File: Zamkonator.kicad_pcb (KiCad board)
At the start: 2 copper layers, 75 x 75 mm, 100 parts, among them J1 Screw_Terminal_01x06, J2 RJ45_Abracon_ARJP11A-MASA-B-A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, J3 Conn_01x08_Male, J4 Conn_02x08_Counter_Clockwise, K1 SRD-DC3V-SL-C, Q1 BCP56, T1 HR051142, U1 RTL8201F, U2 SI3404-A-GM, U3 EL3H7-G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

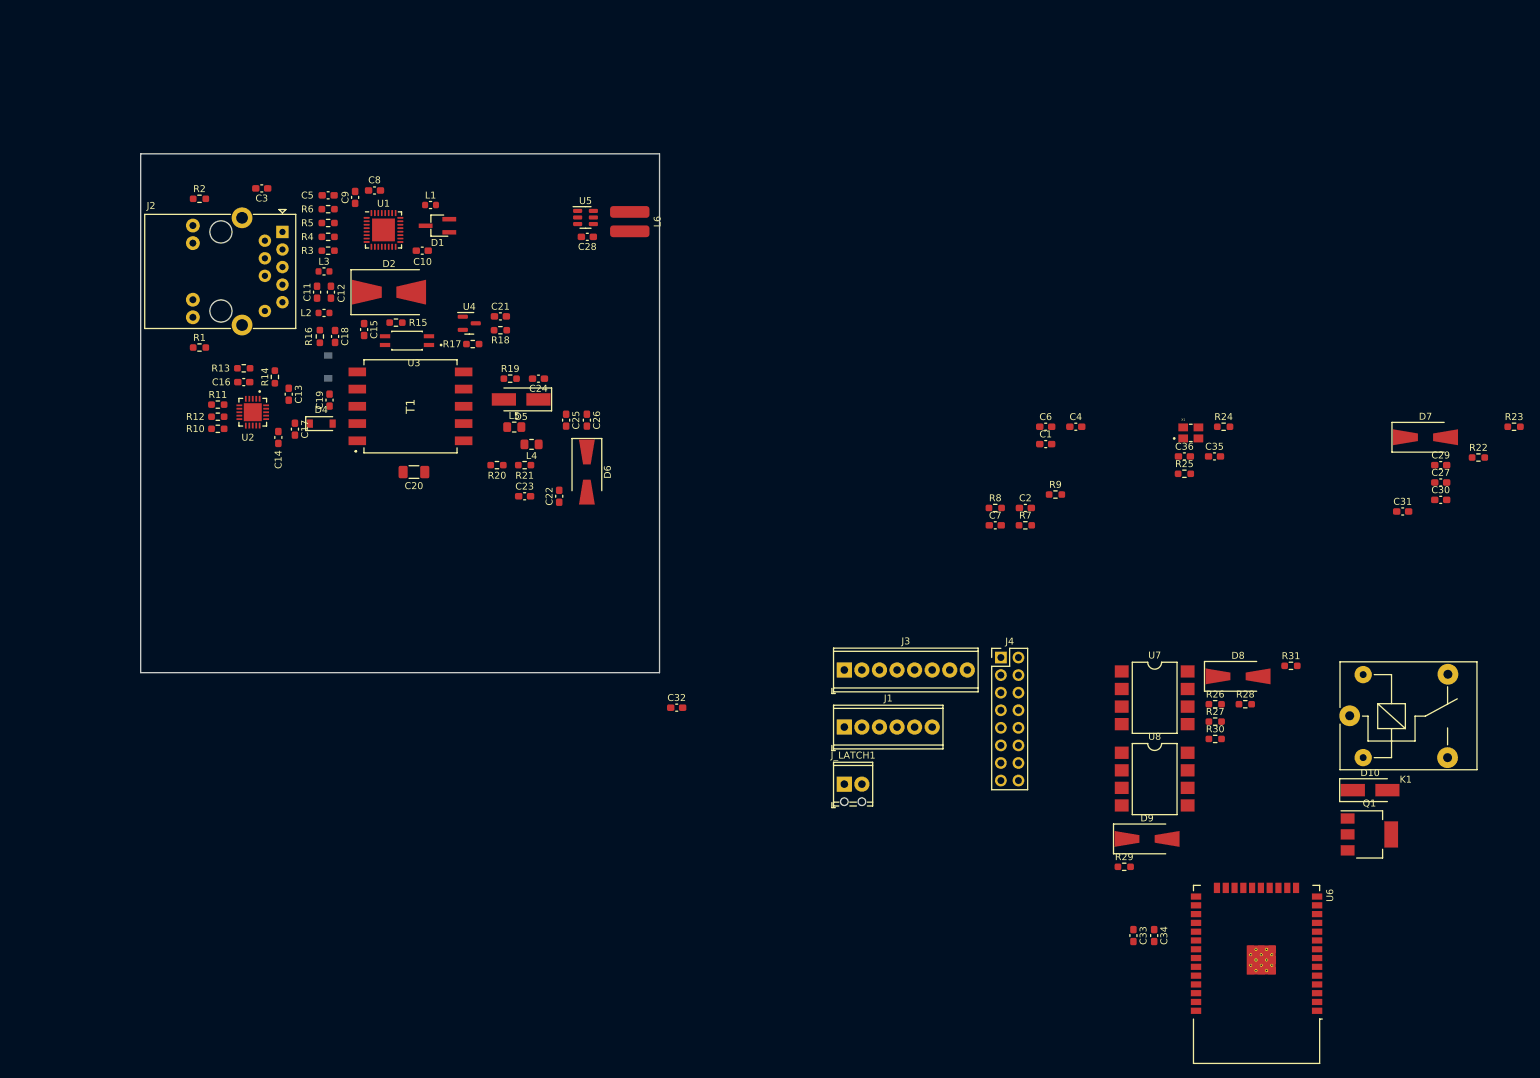
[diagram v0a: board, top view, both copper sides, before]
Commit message: layout fixes
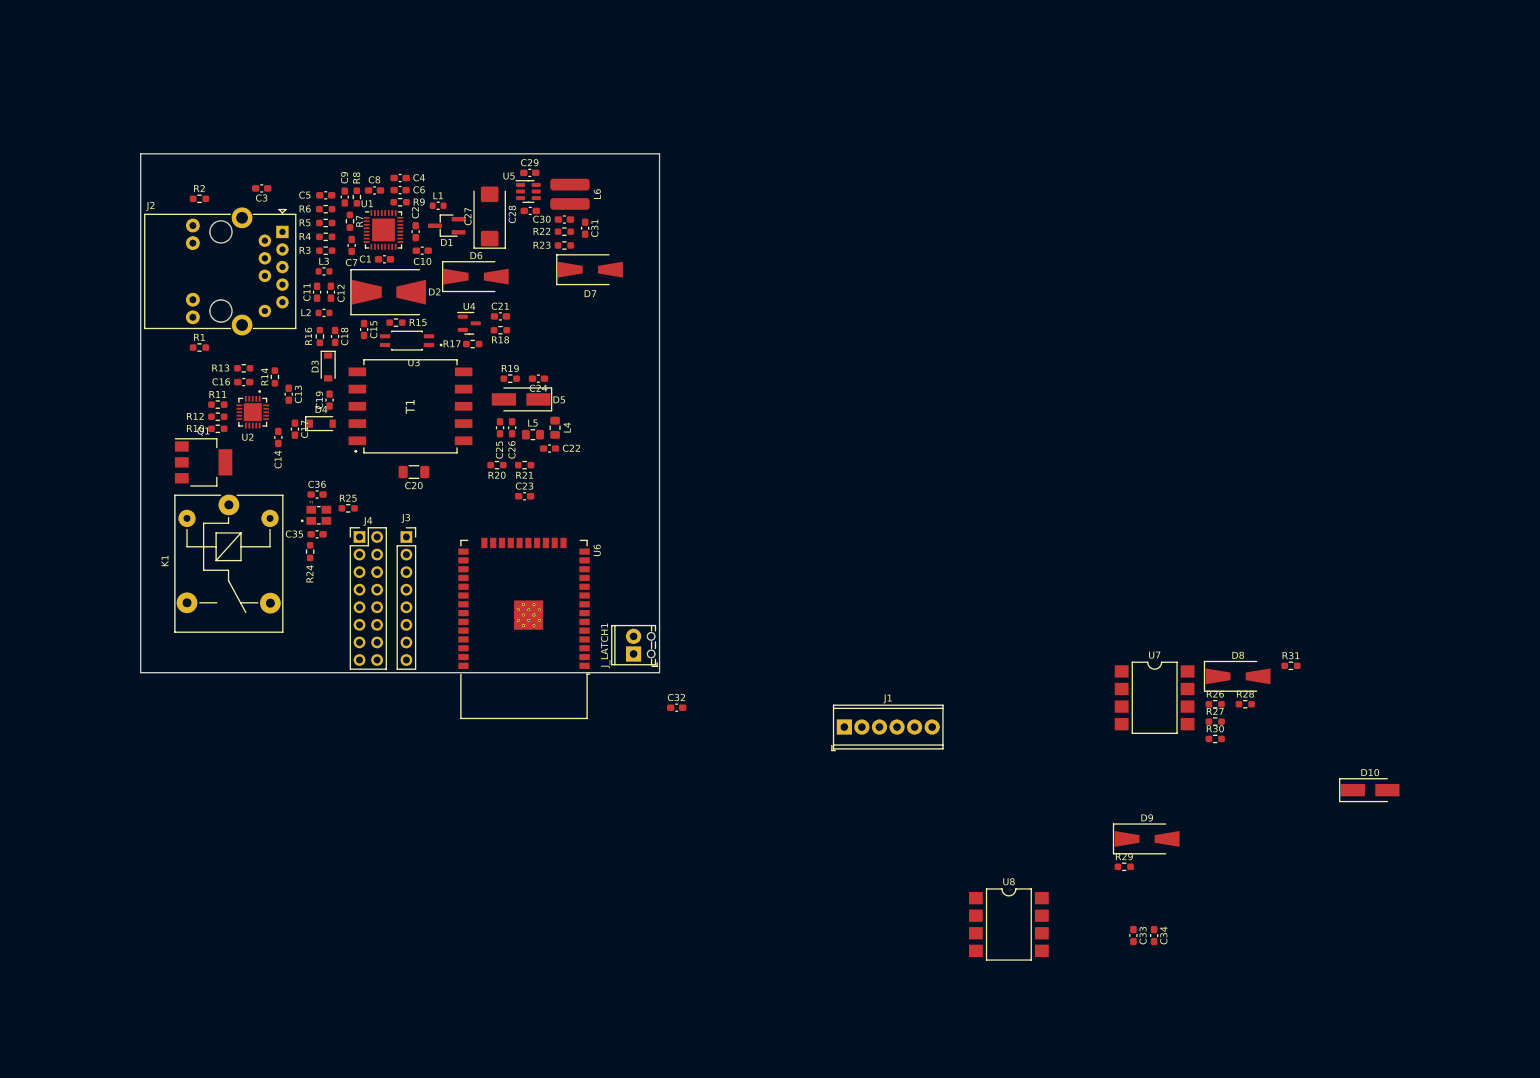
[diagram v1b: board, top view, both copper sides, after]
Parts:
- C27: footprint Capacitor_SMD:C_0603_1608Metric_Pad1.08x0.95mm_HandSolder -> Capacitor_Tantalum_SMD:CP_EIA-7343-30_AVX-N_Pad2.25x2.55mm_HandSolder
- D3: moved to F.Cu
- J3: footprint TerminalBlock_Phoenix:TerminalBlock_Phoenix_MPT-0,5-8-2.54_1x08_P2.54mm_Horizontal -> Connector_PinSocket_2.54mm:PinSocket_1x08_P2.54mm_Vertical
- moved Q1 176.9 mm to (25.6, 63.6)
- moved K1 164.9 mm to (29.2, 69.8), turned to -90 degrees
- moved C27 142.7 mm to (67.0, 28.1), turned to 90 degrees
- moved R23 139.7 mm to (77.8, 32.2)
- moved C29 138.3 mm to (72.8, 21.8)
- moved R22 136.1 mm to (77.8, 30.2), turned to 180 degrees
- moved R24 133.3 mm to (41.0, 76.5), turned to 90 degrees
- moved C30 133.0 mm to (77.8, 28.5), turned to 180 degrees
- moved C35 130.2 mm to (42.0, 74.0)
- moved X1 126.6 mm to (42.2, 71.2)
- moved C36 125.5 mm to (42.0, 68.2)
- moved C31 125.1 mm to (80.8, 29.8), turned to -90 degrees
- moved D7 123.1 mm to (81.5, 35.8)
- moved R25 121.0 mm to (46.5, 70.2)
- moved U6 117.0 mm to (71.9, 84.8)
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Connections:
- X1 pad 2: (no net) -> GND
- X1 pad 3: (no net) -> Net-(R25-Pad1)
- X1 pad 4: (no net) -> +3.3V

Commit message: Finish basic layout
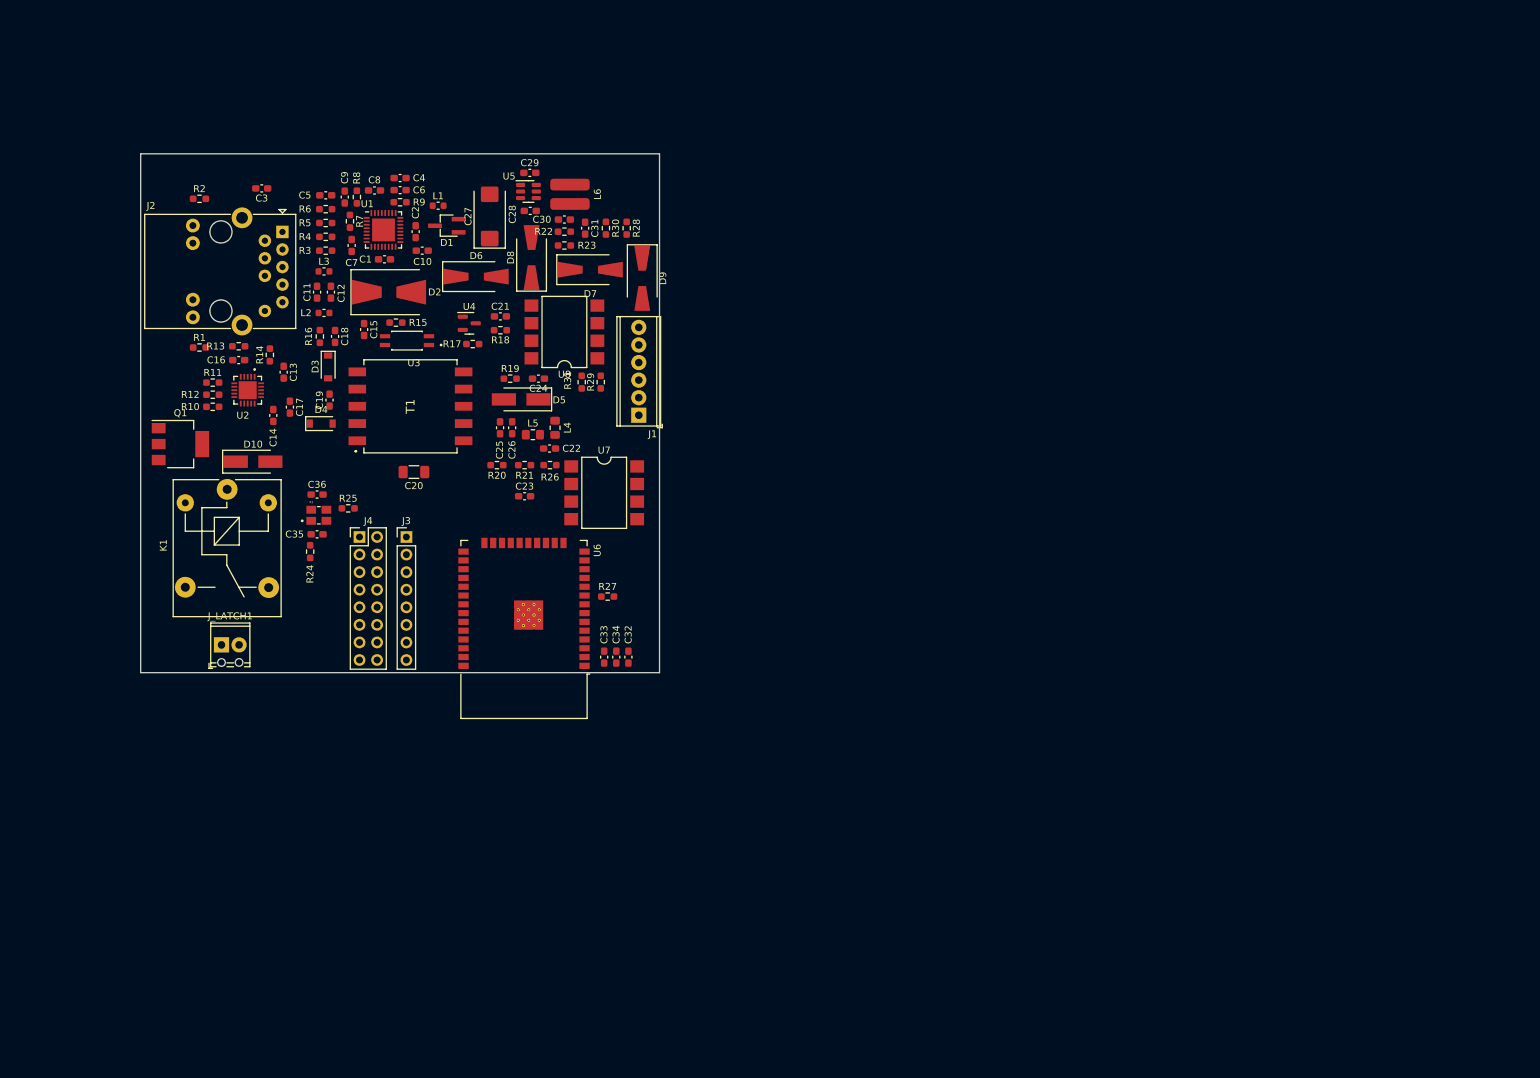
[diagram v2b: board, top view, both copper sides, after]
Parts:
- J3: footprint Connector_PinSocket_2.54mm:PinSocket_1x08_P2.54mm_Vertical -> Connector_PinHeader_2.54mm:PinHeader_1x08_P2.54mm_Vertical
- moved D10 168.3 mm to (32.8, 63.5)
- moved D8 118.7 mm to (73.0, 34.0), turned to 90 degrees
- moved R30 114.9 mm to (83.8, 29.8), turned to -90 degrees
- moved R28 112.8 mm to (86.8, 29.8), turned to -90 degrees
- moved R31 110.4 mm to (80.2, 52.0), turned to -90 degrees
- moved D9 109.0 mm to (89.0, 37.0), turned to -90 degrees
- moved U8 107.1 mm to (77.8, 44.8), turned to 180 degrees
- moved R29 103.1 mm to (83.0, 52.0), turned to 90 degrees
- moved R26 102.2 mm to (75.7, 64.0)
- moved R27 89.7 mm to (84.0, 83.0)
- moved C34 87.6 mm to (85.2, 91.8)
- moved C33 86.4 mm to (83.5, 91.8)
- moved U7 84.9 mm to (83.5, 68.0)
- moved J_LATCH1 59.6 mm to (28.2, 90.0), turned to 0 degrees
- moved J1 54.0 mm to (88.5, 56.8), turned to 90 degrees
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
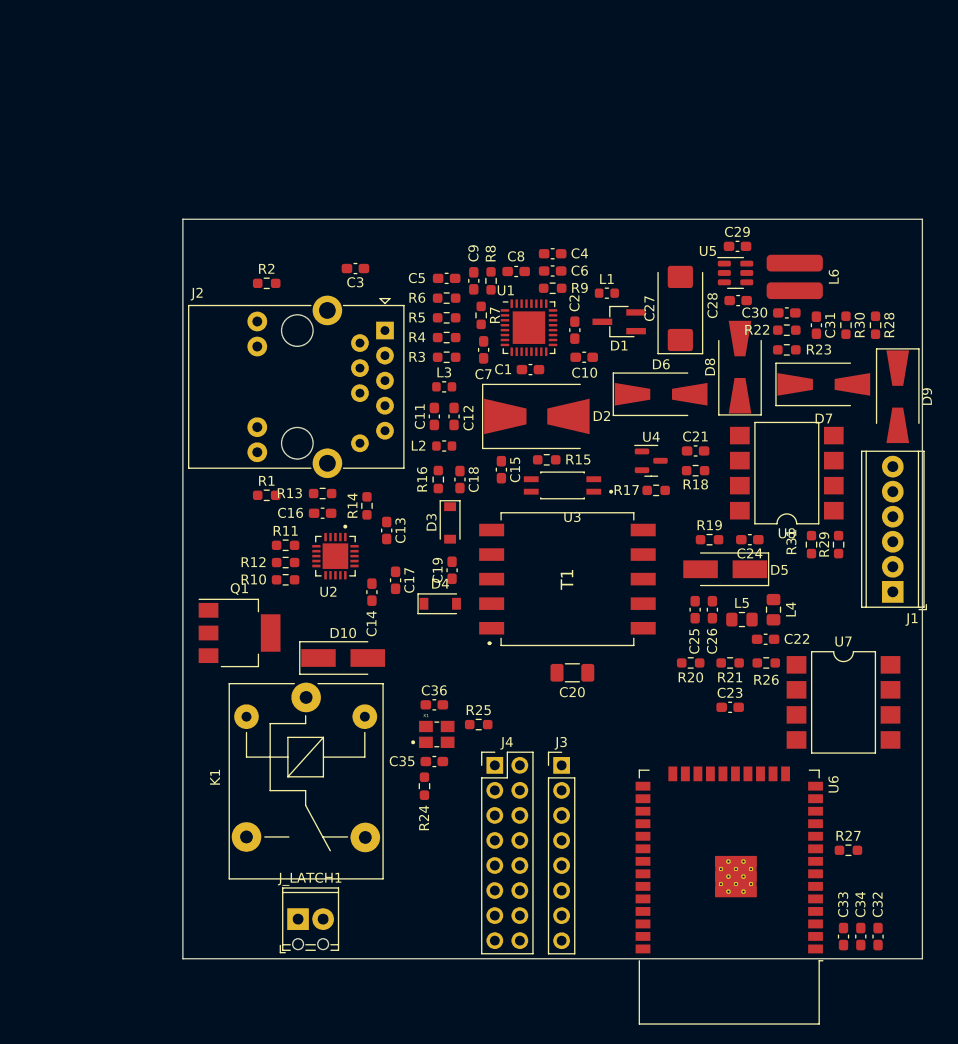
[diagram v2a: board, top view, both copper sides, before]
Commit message: add screw holes
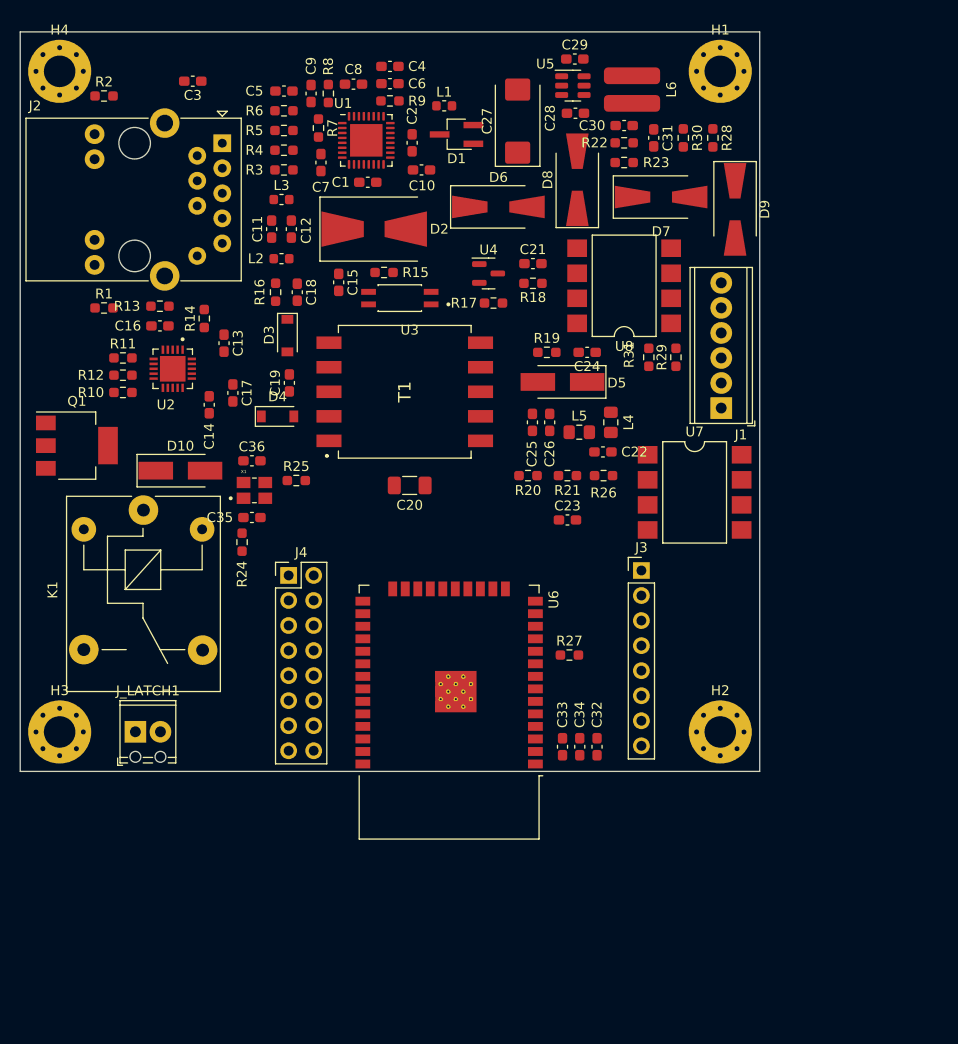
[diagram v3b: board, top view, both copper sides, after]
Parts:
- added H1: MountingHole_Pad, MountingHole:MountingHole_3.2mm_M3_Pad_Via, F.Cu at (71.0, 4.00)
- added H2: MountingHole_Pad, MountingHole:MountingHole_3.2mm_M3_Pad_Via, F.Cu at (71.0, 71.0)
- added H3: MountingHole_Pad, MountingHole:MountingHole_3.2mm_M3_Pad_Via, F.Cu at (4.00, 71.0)
- added H4: MountingHole_Pad, MountingHole:MountingHole_3.2mm_M3_Pad_Via, F.Cu at (4.00, 4.00)
- moved R27 34.5 mm to (55.7, 63.2)
- moved C32 34.4 mm to (58.5, 72.5)
- moved C33 34.4 mm to (55.0, 72.5)
- moved C34 34.4 mm to (56.8, 72.5)
- moved U6 34.0 mm to (43.5, 66.0)
- moved C35 30.9 mm to (23.5, 49.2)
- moved C36 30.9 mm to (23.5, 43.5)
- moved R24 30.9 mm to (22.5, 51.8)
- moved R25 30.9 mm to (28.0, 45.5)
- moved X1 30.9 mm to (23.8, 46.5)
- moved J4 28.4 mm to (27.2, 55.1)
- moved U7 26.1 mm to (68.4, 46.7)
- moved J1 25.5 mm to (71.1, 38.1)
- moved C13 25.2 mm to (20.7, 31.6)
- moved C16 25.2 mm to (14.2, 29.8)
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
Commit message: tracks
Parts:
- moved U6 7.00 mm to (43.2, 59.0)
- moved R27 6.22 mm to (55.2, 57.0)
- moved C32 6.02 mm to (58.0, 66.5)
- moved C33 6.02 mm to (54.5, 66.5)
- moved C34 6.02 mm to (56.2, 66.5)
- moved R7 5.34 mm to (31.2, 15.0), turned to 90 degrees
- moved R15 4.43 mm to (33.0, 26.5), turned to 90 degrees
- moved J_LATCH1 4.30 mm to (16.0, 71.0)
- moved C14 3.26 mm to (22.2, 36.8)
- moved C2 3.09 mm to (40.5, 14.2), turned to 180 degrees
- moved K1 2.75 mm to (9.75, 48.5)
- moved C17 2.40 mm to (19.2, 36.0)
- moved J4 2.26 mm to (25.0, 55.4)
- moved C7 2.02 mm to (29.5, 15.0)
- moved C10 2.01 mm to (40.5, 16.0)
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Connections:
- C1 pad 1: +3V3 -> +3.3V
- C10 pad 1: +3V3 -> +3.3V
- C2 pad 1: +3V3 -> +3.3V
- C32 pad 1: +3V3 -> +3.3V
- D1 pad 2: +3V3 -> +3.3V
- L1 pad 1: +3V3 -> +3.3V
- U1 pad 14: +3V3 -> +3.3V
- U6 pad 2: +3V3 -> +3.3V
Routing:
- net /50MHZ CLOCK/CLK_OUT: track 0.00 -> 93.0 mm, vias 0 -> 2
- net /ESP32/EMAC_RXD1: track 0.00 -> 67.0 mm, vias 0 -> 2
- net /ESP32/EMAC_CRS_DV: track 0.00 -> 62.0 mm, vias 0 -> 2
- net /ESP32/EMAC_MDIO: track 0.00 -> 56.4 mm, vias 0 -> 2
- net Net-(R1-Pad2): track 0.00 -> 56.0 mm, vias 0 -> 2
- net /ESP32/EMAC_TX_EN: track 0.00 -> 54.0 mm, vias 0 -> 2
- net /ESP32/EMAC_MDC: track 0.00 -> 48.7 mm, vias 0 -> 2
- net /ESP32/EMAC_TXD0: track 0.00 -> 48.1 mm, vias 0 -> 2
- net Net-(C12-Pad1): track 0.00 -> 39.5 mm
- net Net-(R2-Pad2): track 0.00 -> 37.4 mm, vias 0 -> 2
- net Net-(C12-Pad2): track 0.00 -> 21.5 mm, vias 0 -> 2
- net Net-(C4-Pad1): track 0.00 -> 21.2 mm
- net Net-(J2-Pad1): track 0.00 -> 21.1 mm
- net Net-(J2-Pad2): track 0.00 -> 18.4 mm, vias 0 -> 1
- net VSS: track 0.00 -> 17.9 mm
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
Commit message: More tracks, before big change in layout...
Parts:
- moved D10 16.7 mm to (20.0, 60.8), turned to -90 degrees
- moved Q1 16.3 mm to (20.6, 48.8), turned to 90 degrees
- moved R9 6.48 mm to (41.1, 12.4), turned to 180 degrees
- moved C35 5.61 mm to (28.3, 52.1)
- moved C36 5.61 mm to (28.3, 46.4)
- moved X1 5.61 mm to (28.6, 49.4)
- moved R25 5.59 mm to (31.8, 49.6), turned to -90 degrees
- moved C23 5.10 mm to (52.3, 44.0), turned to 180 degrees
- moved R24 3.73 mm to (25.4, 49.4), turned to -90 degrees
- moved C22 3.26 mm to (55.9, 43.4)
- moved C25 3.26 mm to (48.8, 40.4)
- moved C26 3.26 mm to (50.5, 40.4)
- moved L4 3.26 mm to (56.7, 40.4)
- moved L5 3.26 mm to (53.5, 41.4)
- moved R20 3.26 mm to (48.3, 45.8)
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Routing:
- net +3.3V: track 16.8 -> 218.6 mm, vias 0 -> 4
- net +12V: track 0.00 -> 172.7 mm, vias 0 -> 3
- net /ESP32/IO23: track 0.00 -> 74.8 mm, vias 0 -> 3
- net /ESP32/EMAC_RXD0: track 0.00 -> 67.4 mm, vias 0 -> 2
- net /ESP32/IO32: track 0.00 -> 61.5 mm, vias 0 -> 3
- net /ESP32/IO35: track 0.00 -> 58.8 mm, vias 0 -> 2
- net /50MHZ CLOCK/CLK_EN: track 0.00 -> 58.3 mm, vias 0 -> 1
- net VSS: track 17.9 -> 66.2 mm, vias 0 -> 2
- net /ESP32/RX: track 0.00 -> 36.3 mm, vias 0 -> 2
- net Net-(D10-Pad1): track 0.00 -> 34.0 mm, vias 0 -> 1
- net /ESP32/TX: track 0.00 -> 30.9 mm, vias 0 -> 1
- net /ESP32/IO15: track 0.00 -> 28.9 mm, vias 0 -> 2
- net Net-(C12-Pad1): track 39.5 -> 67.0 mm, vias 0 -> 2
- net /Wigand Intrerface/READER_LED: track 0.00 -> 26.4 mm, vias 0 -> 1
- net /Wigand Intrerface/READER_BUZZER: track 0.00 -> 25.9 mm, vias 0 -> 1
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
